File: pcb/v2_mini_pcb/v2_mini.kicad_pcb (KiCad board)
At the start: 6 copper layers, 60.8 x 35.1 mm, 113 parts, among them J1 Conn_Coaxial, J2 GTFP08441BEU, J3 SFV24R-2STE1HLF, J5 TC2030, J6 USB4105-GF-A, Q1 NTNS3164NZT5G, SW1 SW_Push, SW2 SW_Push, SW3 SW_Push, SW4 SW_Push, SW5 SW_Push, SW6 SW_Push, U1 UM980, U10 TPS63802DLAR, U3 SCH16T-K01-1, U4 LP5813ADRRR, U5 TCA9536ADTMR, U6 TPD4EUSB30, U8 BQ25622ERYKR, U9 MAX17048G_T10

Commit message: update footprints
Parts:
- J1: footprint Connector_Coaxial:U.FL_Hirose_U.FL-R-SMT-1_Vertical -> all:U.FL_Hirose_U.FL-R-SMT-1_Vertical
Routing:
- net /ESP32-S31 MCU/LCD_BACK: track 32.7 -> 32.0 mm

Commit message: move buttons
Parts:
- moved SW5 11.1 mm to (132.7, 106.6), turned to 180 degrees
- moved SW3 10.4 mm to (127.2, 102.2), turned to -90 degrees
- moved SW6 6.32 mm to (121.7, 106.9), turned to 180 degrees
- moved H6 5.70 mm to (133.3, 110.9)
- moved U5 4.48 mm to (122.2, 110.3)
- moved SW4 1.20 mm to (127.2, 110.8)
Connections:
- J5 pad 1: +3V3 -> unconnected-(J5-Pad1)
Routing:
- net Net-(U5-P3/INT): track 2.43 -> 12.0 mm
- net GND: track 96.9 -> 102.8 mm, vias 255 -> 261
- net Net-(U5-P0): track 12.5 -> 7.70 mm
- net Net-(U5-P1): track 8.09 -> 3.58 mm
- net /ESP32-S31 MCU/POW_SDA: track 104.2 -> 108.7 mm
- net /ESP32-S31 MCU/POW_SCL: track 102.2 -> 106.4 mm
- net +3V3: track 56.9 -> 52.9 mm
- net Net-(U5-P2): track 6.48 -> 5.02 mm

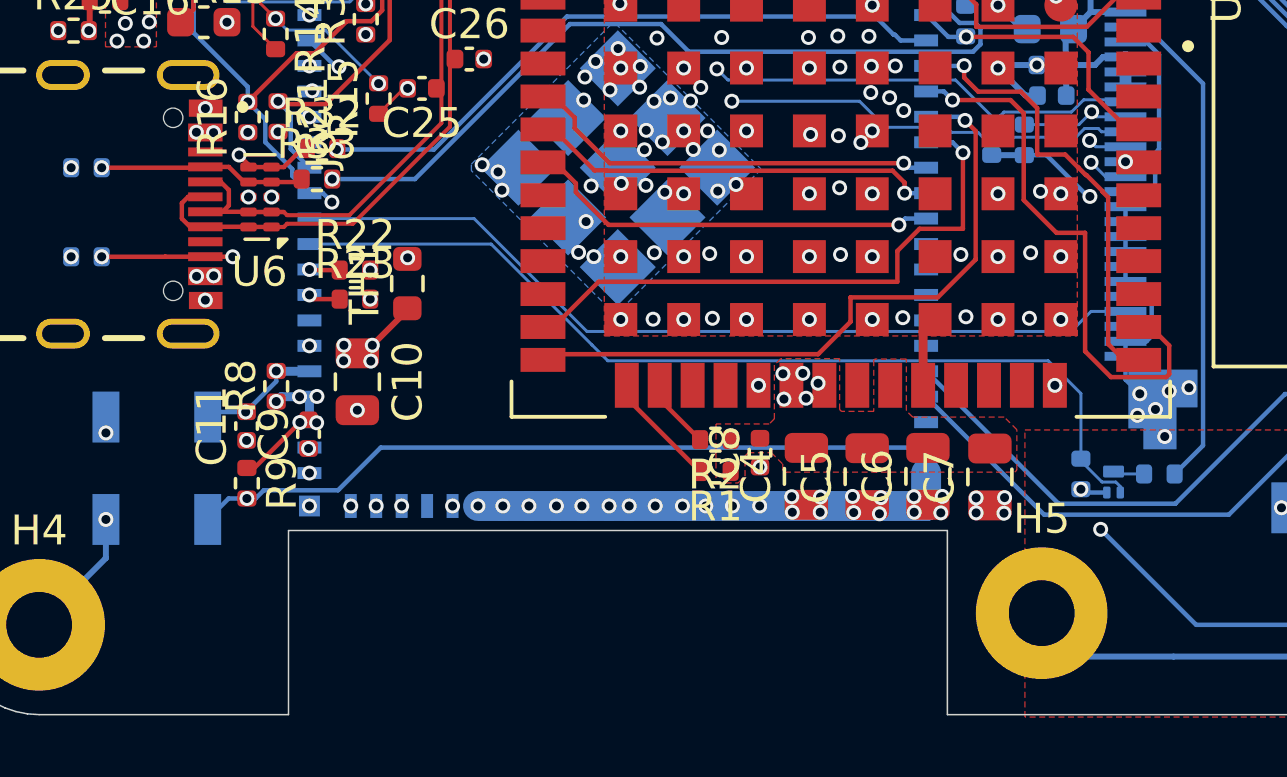
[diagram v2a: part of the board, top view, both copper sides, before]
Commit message: add power off schematic
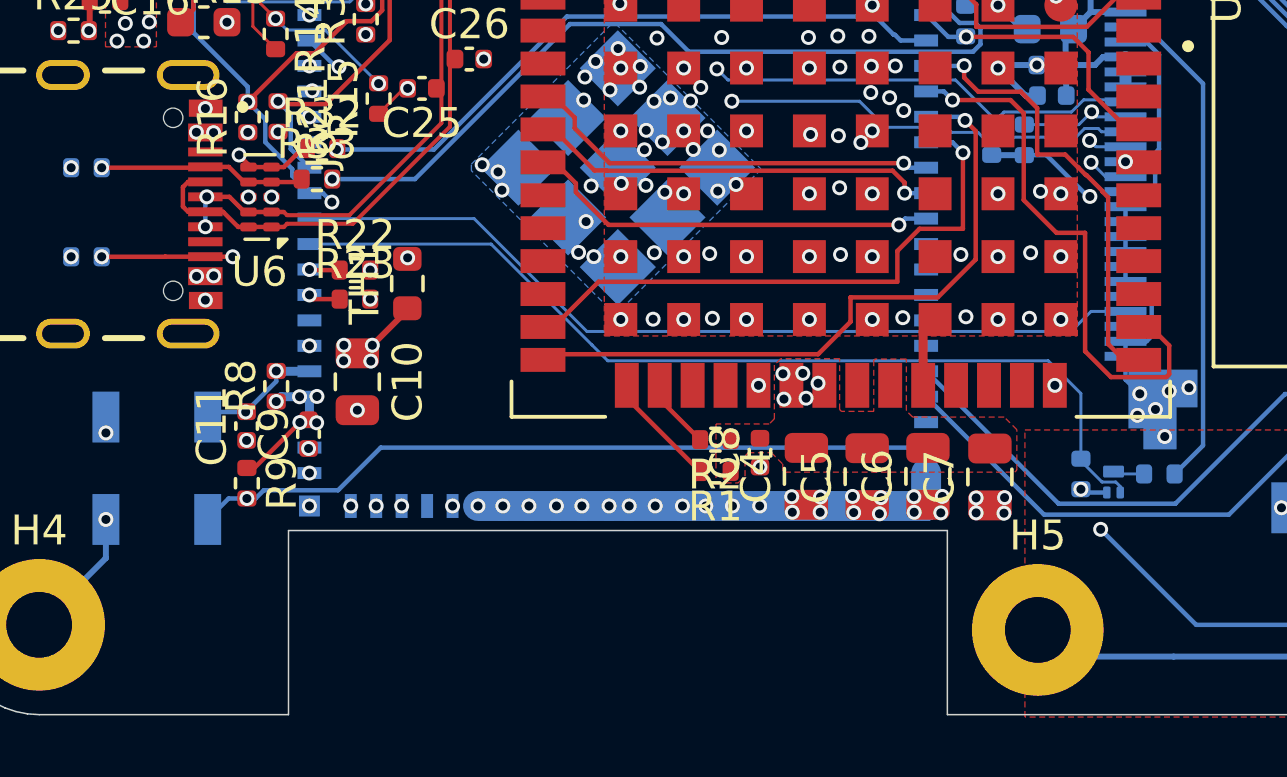
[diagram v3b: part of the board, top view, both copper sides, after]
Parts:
- moved H5 0.57 mm to (111.7, 110.9)
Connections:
- C25 pad 1: /ESP32-S31 MCU/USB_DP -> /ESP32-S31 MCU/USB_DN
- C26 pad 1: /ESP32-S31 MCU/USB_DN -> /ESP32-S31 MCU/USB_DP
- J6 pad A6: /ESP32-S31 MCU/USB_DN -> /ESP32-S31 MCU/USB_DP
- J6 pad A7: /ESP32-S31 MCU/USB_DP -> /ESP32-S31 MCU/USB_DN
- J6 pad B6: /ESP32-S31 MCU/USB_DN -> /ESP32-S31 MCU/USB_DP
- J6 pad B7: /ESP32-S31 MCU/USB_DP -> /ESP32-S31 MCU/USB_DN
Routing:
- net /ESP32-S31 MCU/USB_DP: track 27.7 -> 26.5 mm, vias 0 -> 2
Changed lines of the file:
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@@
 			(size 0.3 1.15)
 			(layers "F.Cu" "F.Paste")
-			(net "/ESP32-S31 MCU/USB_DN")
+			(net "/ESP32-S31 MCU/USB_DP")
 			(pinfunction "DP1_A6")
 			(pintype "bidirectional")
@@
 			(size 0.3 1.15)
 			(layers "F.Cu" "F.Paste")
-			(net "/ESP32-S31 MCU/USB_DP")
+			(net "/ESP32-S31 MCU/USB_DN")
 			(pinfunction "DN1_A7")
 			(pintype "bidirectional")
@@
 			(size 0.3 1.15)
 			(layers "F.Cu" "F.Paste")
-			(net "/ESP32-S31 MCU/USB_DN")
+			(net "/ESP32-S31 MCU/USB_DP")
 			(pinfunction "DP2_B6")
 			(pintype "bidirectional")
@@
 			(size 0.3 1.15)
 			(layers "F.Cu" "F.Paste")
-			(net "/ESP32-S31 MCU/USB_DP")
+			(net "/ESP32-S31 MCU/USB_DN")
 			(pinfunction "DN2_B7")
 			(pintype "bidirectional")
@@
 			(unit
 				(name "A")
-				(pins "1" "10" "2" "9" "3" "8" "4" "7" "5" "6")
+				(pins "2" "9" "1" "10" "3" "8" "4" "7" "5" "6")
 			)
 		)
@@
 	(footprint "MountingHole:MountingHole_2.2mm_M2_Pad"
 		(layer "F.Cu")
-		(at 111.83 110.38)
+		(at 111.7 110.94)
 		(descr "Mounting Hole 2.2mm, M2, generated by kicad-footprint-generator mountinghole.py")
 		(tags "mountinghole M2")
@@
 			(layers "F.Cu" "F.Mask" "F.Paste")
 			(roundrect_rratio 0.25)
-			(net "/ESP32-S31 MCU/USB_DP")
+			(net "/ESP32-S31 MCU/USB_DN")
 			(pintype "passive")
 		)
@@
 			(layers "F.Cu" "F.Mask" "F.Paste")
 			(roundrect_rratio 0.25)
-			(net "/ESP32-S31 MCU/USB_DN")
+			(net "/ESP32-S31 MCU/USB_DP")
 			(pintype "passive")
 		)
@@
 	)
 	(point
-		(at 127.16 102.41)
+		(at 107.97 97.2)
 		(size 1)
-		(layer "F.Cu")
+		(layer "B.Cu")
 	)
 	(point
-		(at 107.97 97.2)
+		(at 107.97 98.9)
 		(size 1)
 		(layer "B.Cu")
@@
 	)
 	(point
-		(at 107.97 98.9)
+		(at 131.07 110.86)
+		(size 1)
+		(layer "B.Cu")
+	)
+	(point
+		(at 133.27 110.86)
+		(size 1)
+		(layer "B.Cu")
+	)
+	(point
+		(at 133.27 110.86)
+		(size 1)
+		(layer "B.Cu")
+	)
+	(point
+		(at 133.27 110.86)
+		(size 1)
+		(layer "B.Cu")
+	)
+	(point
+		(at 133.27 110.86)
+		(size 1)
+		(layer "B.Cu")
+	)
+	(point
+		(at 133.27 110.86)
+		(size 1)
+		(layer "B.Cu")
+	)
+	(point
+		(at 133.27 110.86)
+		(size 1)
+		(layer "B.Cu")
+	)
+	(point
+		(at 133.27 110.86)
+		(size 1)
+		(layer "B.Cu")
+	)
+	(point
+		(at 133.27 110.86)
+		(size 1)
+		(layer "B.Cu")
+	)
+	(point
+		(at 133.27 110.86)
+		(size 1)
+		(layer "B.Cu")
+	)
+	(point
+		(at 133.27 110.86)
 		(size 1)
 		(layer "B.Cu")
@@
 	)
 	(segment
-		(start 86.10312 97.478822)
-		(end 86.515621 97.478822)
-		(width 0.1356)
-		(layer "F.Cu")
-		(net "/ESP32-S31 MCU/USB_DN")
-	)
-	(segment
 		(start 86.515621 97.478822)
 		(end 86.622821 97.371622)
@@
 	)
 	(segment
-		(start 85.123822 97.478822)
-		(end 85.33312 97.478822)
-		(width 0.15)
+		(start 86.622821 97.371622)
+		(end 88.820328 97.371622)
+		(width 0.1356)
 		(layer "F.Cu")
 		(net "/ESP32-S31 MCU/USB_DN")
 	)
 	(segment
-		(start 86.622821 97.371622)
-		(end 88.820328 97.371622)
-		(width 0.1356)
+		(start 83.1425 96.1475)
+		(end 83.3175 95.9725)
+		(width 0.15)
 		(layer "F.Cu")
 		(net "/ESP32-S31 MCU/USB_DN")
@@
 	)
 	(segment
-		(start 83.1075 96.6825)
-		(end 83.3175 96.4725)
+		(start 86.515621 97.478822)
+		(end 86.10312 97.478822)
 		(width 0.15)
 		(layer "F.Cu")
@@
 	)
 	(segment
-		(start 83.8925 97.4725)
-		(end 83.38 97.4725)
+		(start 83.3175 95.9725)
+		(end 83.8925 95.9725)
 		(width 0.15)
 		(layer "F.Cu")
@@
 	)
 	(segment
-		(start 94.64915 86.7428)
-		(end 100.15915 86.7428)
-		(width 0.1356)
+		(start 83.8925 96.9725)
+		(end 83.3175 96.9725)
+		(width 0.15)
 		(layer "F.Cu")
 		(net "/ESP32-S31 MCU/USB_DN")
 	)
 	(segment
-		(start 92.0628 89.32915)
-		(end 94.64915 86.7428)
-		(width 0.1356)
+		(start 83.8925 96.9725)
+		(end 84.4825 96.9725)
+		(width 0.15)
 		(layer "F.Cu")
 		(net "/ESP32-S31 MCU/USB_DN")
 	)
 	(segment
-		(start 92.0628 94.12915)
-		(end 92.0628 89.32915)
+		(start 94.64915 86.7428)
+		(end 100.15915 86.7428)
 		(width 0.1356)
 		(layer "F.Cu")
@@
 	)
 	(segment
-		(start 88.820328 97.371622)
-		(end 92.0628 94.12915)
-		(width 0.1356)
+		(start 83.3175 96.9725)
+		(end 83.1425 96.7975)
+		(width 0.15)
 		(layer "F.Cu")
 		(net "/ESP32-S31 MCU/USB_DN")
 	)
 	(segment
-		(start 83.3175 96.4725)
-		(end 83.8925 96.4725)
+		(start 84.988822 97.478822)
+		(end 85.33312 97.478822)
 		(width 0.15)
 		(layer "F.Cu")
@@
 	)
 	(segment
-		(start 83.38 97.4725)
-		(end 83.1075 97.2)
+		(start 83.1425 96.7975)
+		(end 83.1425 96.1475)
 		(width 0.15)
 		(layer "F.Cu")
@@
 	)
 	(segment
-		(start 83.8925 97.4725)
-		(end 85.326798 97.4725)
-		(width 0.15)
+		(start 92.0628 89.32915)
+		(end 94.64915 86.7428)
+		(width 0.1356)
 		(layer "F.Cu")
 		(net "/ESP32-S31 MCU/USB_DN")
 	)
 	(segment
-		(start 83.1075 97.2)
-		(end 83.1075 96.6825)
+		(start 84.4825 96.9725)
+		(end 84.988822 97.478822)
 		(width 0.15)
 		(layer "F.Cu")
@@
 	)
 	(segment
+		(start 92.0628 94.12915)
+		(end 92.0628 89.32915)
+		(width 0.1356)
+		(layer "F.Cu")
+		(net "/ESP32-S31 MCU/USB_DN")
+	)
+	(segment
+		(start 88.820328 97.371622)
+		(end 92.0628 94.12915)
+		(width 0.1356)
+		(layer "F.Cu")
+		(net "/ESP32-S31 MCU/USB_DN")
+	)
+	(segment
 		(start 107.195 83.085)
 		(end 107.17 83.06)
@@
 	)
 	(segment
-		(start 84.4675 96.9725)
-		(end 83.8925 96.9725)
-		(width 0.15)
-		(layer "F.Cu")
-		(net "/ESP32-S31 MCU/USB_DP")
-	)
-	(segment
-		(start 84.405 95.9725)
-		(end 84.6775 96.245)
+		(start 84.696166 96.4725)
+		(end 85.202488 96.978822)
 		(width 0.15)
 		(layer "F.Cu")
@@
 	)
 	(segment
-		(start 83.8925 95.9725)
-		(end 84.405 95.9725)
-		(width 0.15)
-		(layer "F.Cu")
-		(net "/ESP32-S31 MCU/USB_DP")
-	)
-	(segment
-		(start 83.8925 96.9725)
-		(end 85.326798 96.9725)
+		(start 85.202488 96.978822)
+		(end 85.33312 96.978822)
 		(width 0.15)
 		(layer "F.Cu")
@@
 	)
 	(segment
-		(start 84.6775 96.7625)
-		(end 84.4675 96.9725)
+		(start 83.8925 96.4725)
+		(end 83.94 96.4725)
 		(width 0.15)
 		(layer "F.Cu")
@@
 	)
 	(segment
-		(start 85.33312 96.978822)
+		(start 86.515621 96.978822)
 		(end 86.10312 96.978822)
 		(width 0.15)
@@
 	)
 	(segment
-		(start 84.6775 96.245)
-		(end 84.6775 96.7625)
+		(start 85.33312 96.978822)
+		(end 86.10312 96.978822)
 		(width 0.15)
 		(layer "F.Cu")
@@
 	)
 	(segment
-		(start 85.202488 96.978822)
-		(end 85.33312 96.978822)
+		(start 83.94 96.4725)
+		(end 84.696166 96.4725)
 		(width 0.15)
 		(layer "F.Cu")
@@
 	)
 	(segment
-		(start 86.515621 96.978822)
-		(end 86.10312 96.978822)
+		(start 85.43 96.9725)
+		(end 85.445 96.9875)
 		(width 0.15)
 		(layer "F.Cu")
 		(net "/ESP32-S31 MCU/USB_DP")
 	)
+	(via
+		(at 83.8925 97.4725)
+		(size 0.5)
+		(drill 0.3)
+		(layers "F.Cu" "B.Cu")
+		(net "/ESP32-S31 MCU/USB_DP")
+	)
+	(via
+		(at 83.94 96.4725)
+		(size 0.5)
+		(drill 0.3)
+		(layers "F.Cu" "B.Cu")
+		(net "/ESP32-S31 MCU/USB_DP")
+	)
 	(segment
-		(start 85.43 96.9725)
-		(end 85.445 96.9875)
+		(start 83.8925 97.4725)
+		(end 83.8925 96.52)
 		(width 0.15)
-		(layer "F.Cu")
+		(layer "B.Cu")
+		(net "/ESP32-S31 MCU/USB_DP")
+	)
+	(segment
+		(start 83.8925 96.52)
+		(end 83.94 96.4725)
+		(width 0.15)
+		(layer "B.Cu")
 		(net "/ESP32-S31 MCU/USB_DP")
 	)

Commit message: add power button to pcb
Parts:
- added C41: 100nF, Capacitor_SMD:C_0402_1005Metric, B.Cu at (82.2, 88.2)
- added R34: 10k, Resistor_SMD:R_0402_1005Metric, B.Cu at (84.2, 88.2)
- added R35: 10k, Resistor_SMD:R_0402_1005Metric, B.Cu at (94.7, 82.5)
- added SW7: SW_Push, Button_Switch_SMD:SW_SPST_B3U-1000P, B.Cu at (80.3, 85.9)
- added U7: MAX16169AALTA+T, all:21-0164_L622&plus_1_ADI, B.Cu at (84.6, 86.1)
- moved C25 1.86 mm to (92.7, 91.9), turned to 0 degrees
- moved C26 1.86 mm to (91.1, 92.8), turned to 180 degrees
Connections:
- U10 pad 1: /Power + USB/3V3_RAW -> /Power + USB/GATE_EN
- U2 pad 14: unconnected-(U2-GPIO8-Pad14) -> /ESP32-S31 MCU/PWR_KILL_N
- U2 pad 49: unconnected-(U2-GPIO38-Pad49) -> /ESP32-S31 MCU/PWR_INT_N
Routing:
- net /ESP32-S31 MCU/PWR_INT_N: track 0.00 -> 27.1 mm, vias 0 -> 2
- net /ESP32-S31 MCU/PWR_KILL_N: track 0.00 -> 12.9 mm
- net /Power + USB/GATE_EN: track 0.00 -> 7.91 mm, vias 0 -> 1
- net /Power + USB/3V3_RAW: track 0.00 -> 6.16 mm, vias 0 -> 1
- net GND: track 102.8 -> 105.4 mm, vias 261 -> 262
- net Net-(U7-PB_IN/*PB_IN): track 0.00 -> 2.09 mm
- net /ESP32-S31 MCU/POW_SCL: track 106.4 -> 108.3 mm
- net +3V3: track 52.9 -> 54.3 mm, vias 25 -> 26

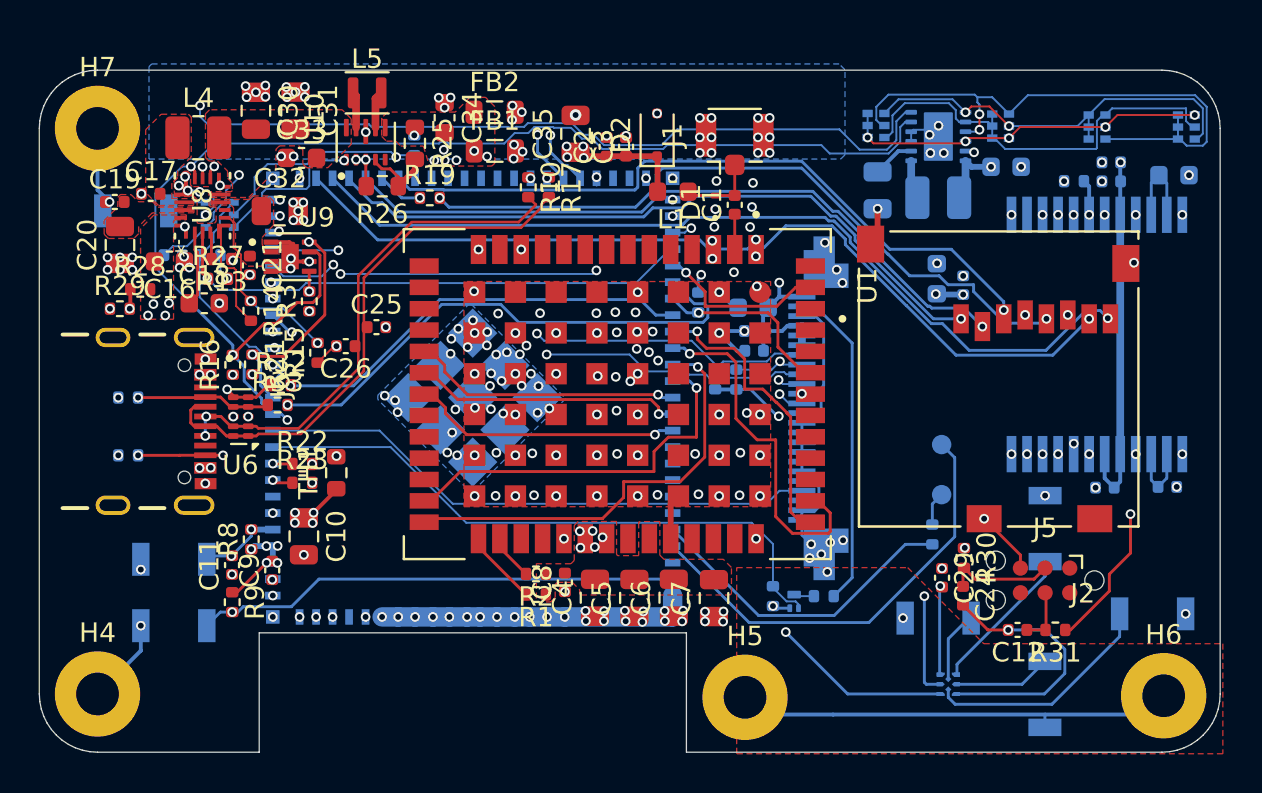
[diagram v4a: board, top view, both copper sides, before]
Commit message: length tune sdio
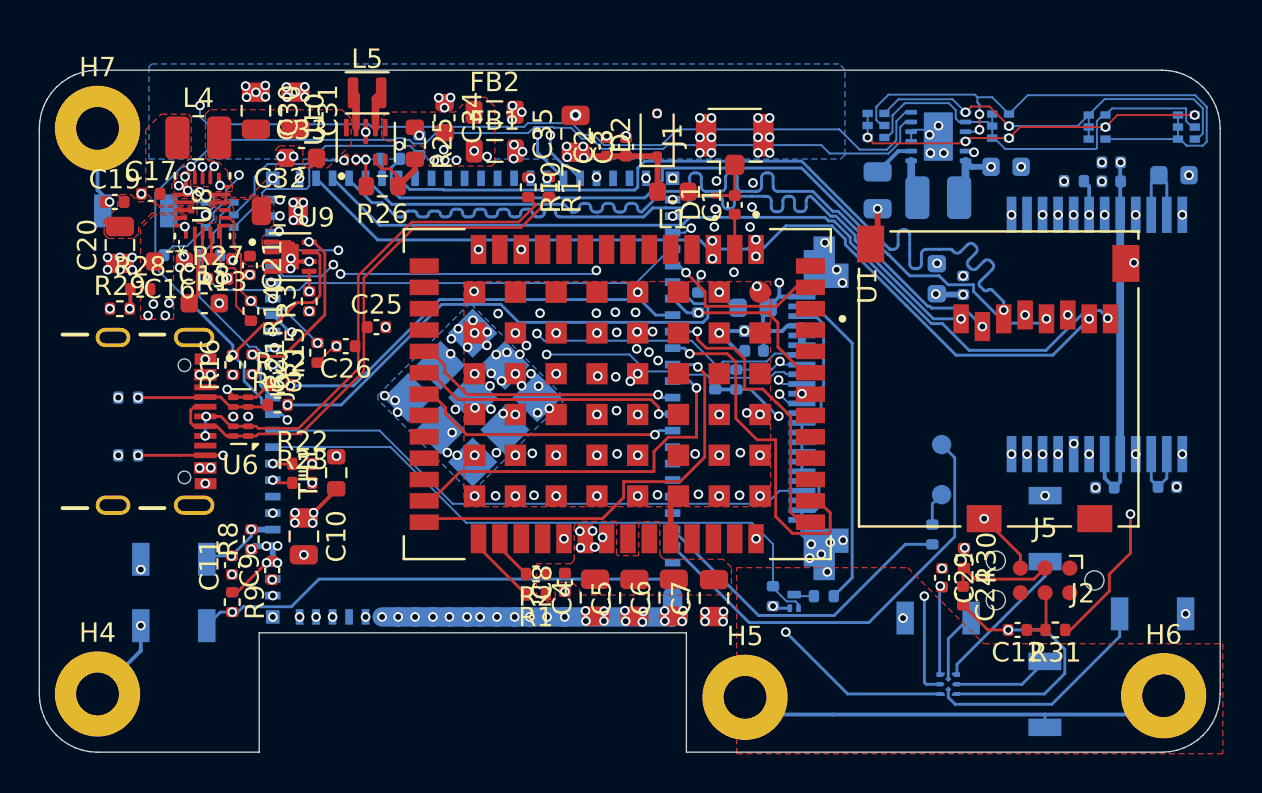
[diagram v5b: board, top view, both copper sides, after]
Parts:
- R19: moved to B.Cu
- moved R19 2.86 mm to (93.4, 83.2)
- moved R35 0.26 mm to (94.9, 82.5)
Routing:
- net /ESP32-S31 MCU/SD_CMD: track 36.0 -> 43.0 mm
- net /ESP32-S31 MCU/SD_D2: track 35.6 -> 41.5 mm
- net /ESP32-S31 MCU/SD_D3: track 36.0 -> 41.8 mm
- net Net-(J2-CLK): track 36.3 -> 40.3 mm, vias 2 -> 1
- net /ESP32-S31 MCU/SD_CLK: track 2.37 -> 1.04 mm, vias 1 -> 0

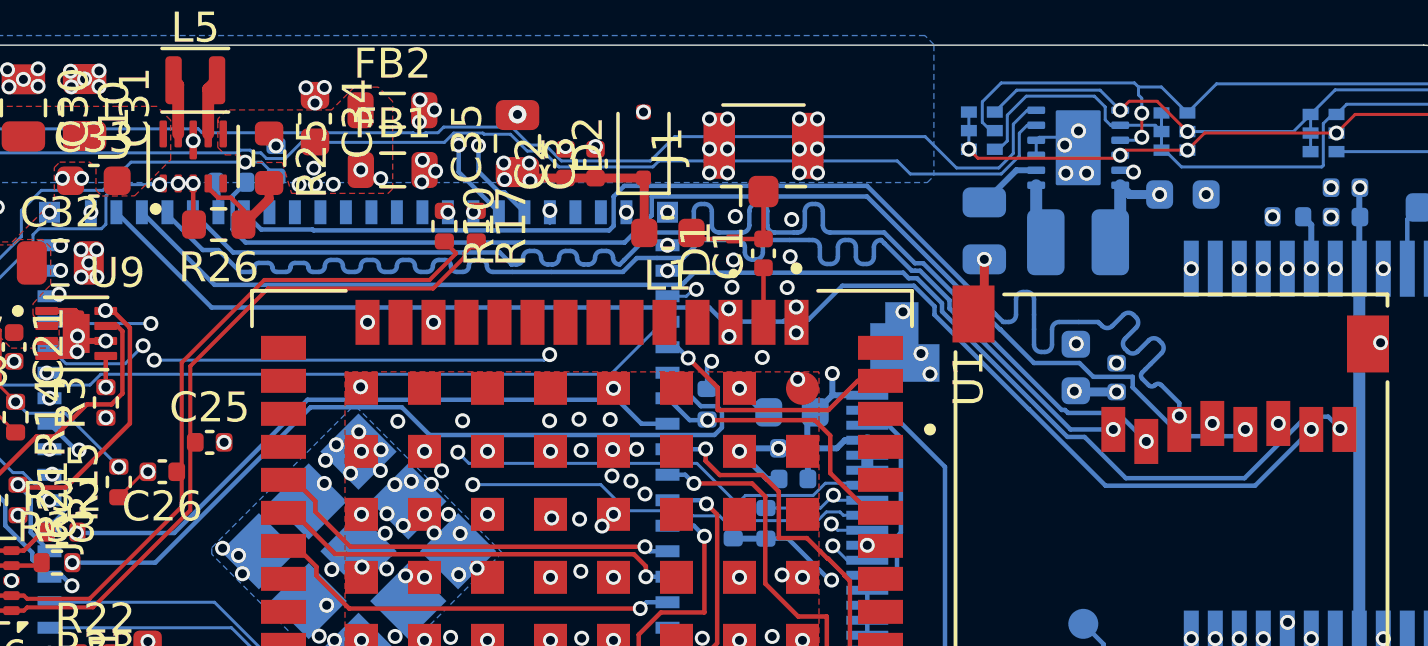
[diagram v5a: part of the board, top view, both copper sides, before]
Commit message: better length tune
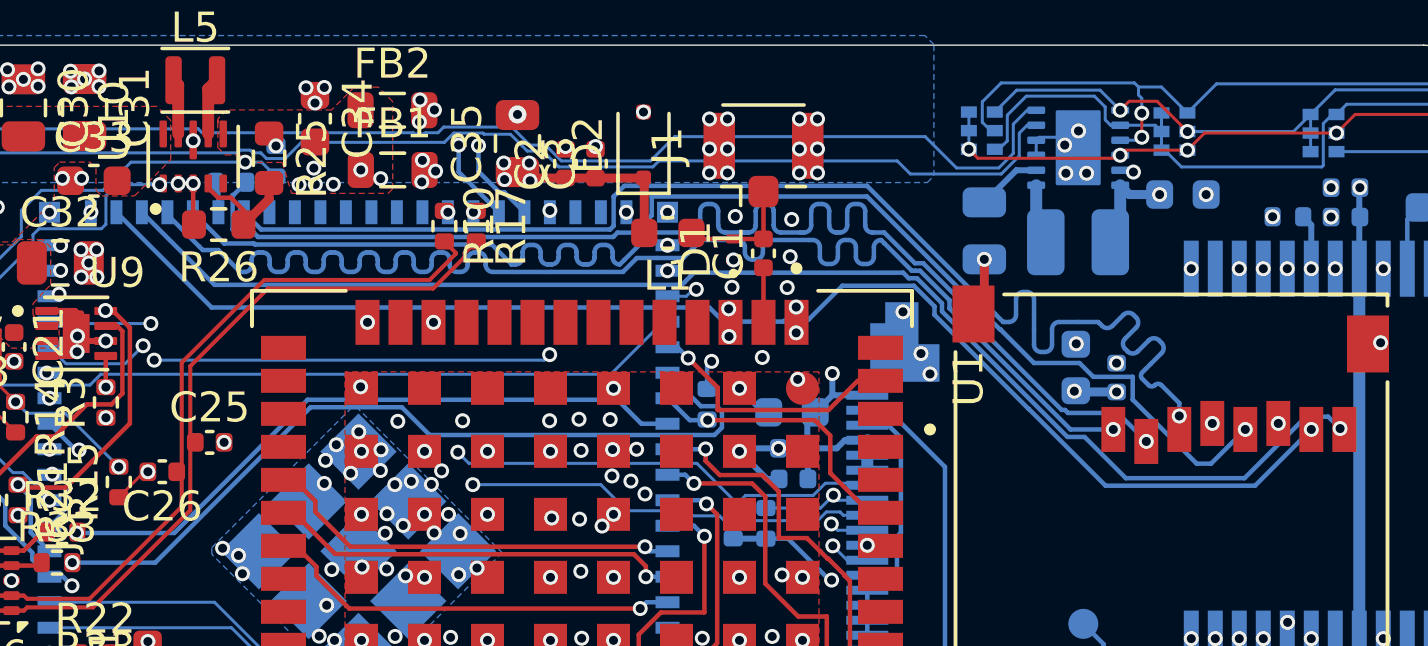
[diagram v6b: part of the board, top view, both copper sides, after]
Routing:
- net /ESP32-S31 MCU/SD_D2: track 41.5 -> 44.7 mm
- net /ESP32-S31 MCU/SD_D3: track 41.8 -> 44.3 mm
- net Net-(J2-CLK): track 40.3 -> 41.2 mm
